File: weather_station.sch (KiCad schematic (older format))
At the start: 32 parts, among them J1 Conn_02x10_Odd_Even, J2 Conn_02x10_Odd_Even, U3 nRF52832, Y1 FL3200037

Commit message: updates
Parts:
- added C29, C30: C_Small, Capacitors_SMD:C_0402, symbol C_Small
- added J4: Conn_Coaxial, Connectors:SMA_SMD_Jack_Straight, symbol Conn_Coaxial
- added Y2: 32.786khz, Crystals:Crystal_SMD_EuroQuartz_EQ161-2pin_3.2x1.5mm, symbol Crystal
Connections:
- net GND: now also C29.2, C30.1, J4.2 (Ext)
- net RADIO_DATA: now also U3.18 (P0.15/TRACEDATA[2]); no longer U3.17 (P0.14/TRACEDATA[3])
- net RADIO_PTT: now also U3.17 (P0.14/TRACEDATA[3]); no longer U3.16 (P0.13)
- net RADIO_UART_RX: now also U3.20 (P0.17); no longer U3.19 (P0.16/TRACEDATA[1])
- net RADIO_UART_TX: now also U3.19 (P0.16/TRACEDATA[1]); no longer U3.18 (P0.15/TRACEDATA[2])
- net ANEOMETER: now reaches U3.10 (P0.08)
- net XL1: now reaches U3.2 (P0.00/XL1)
- net XL1: now also C30.2, Y2.2
- net XL2: now reaches U3.3 (P0.01/XL2)
- net XL2: now also C29.1, Y2.1
- net at C12.2, L3.1, L4.2: now also J4.1 (In)
- new net RADIO_PD: U3.16 (P0.13)
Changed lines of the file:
@@
 $EndComp
 Wire Wire Line
-	7740 1530 7660 1530
+	7100 1530 7740 1530
 Wire Wire Line
 	7660 1510 7660 1600
@@
 Text GLabel 10550 2900 1    60   Input ~ 0
 SWDIO
-Text GLabel 6900 4400 2    60   Input ~ 0
+Text GLabel 6900 4300 2    60   Input ~ 0
 RADIO_UART_TX
-Text GLabel 6900 4300 2    60   Input ~ 0
+Text GLabel 6900 4200 2    60   Input ~ 0
 RADIO_UART_RX
 Text GLabel 10400 4600 1    60   Input ~ 0
@@
 	0    1    1    0
 $EndComp
-Text GLabel 6900 4600 2    60   Input ~ 0
+Text GLabel 6900 4500 2    60   Input ~ 0
 RADIO_PTT
 Text GLabel 6900 2900 2    60   Input ~ 0
@@
 Entry Wire Line
 	-450 4100 -350 4200
-Text GLabel 6900 4500 2    60   Input ~ 0
+Text GLabel 6900 4400 2    60   Input ~ 0
 RADIO_DATA
 Text GLabel 6900 4700 2    60   Input ~ 0
@@
 Text GLabel 6900 3600 2    60   Input ~ 0
 SWDIO
+Text GLabel 6900 4600 2    60   Input ~ 0
+RADIO_PD
+$Comp
+L Crystal Y2
+U 1 1 5A788BD1
+P 2300 3550
+F 0 "Y2" H 2300 3700 50  0000 C CNN
+F 1 "32.786khz" H 2300 3400 50  0000 C CNN
+F 2 "Crystals:Crystal_SMD_EuroQuartz_EQ161-2pin_3.2x1.5mm" H 2300 3550 50  0001 C CNN
+F 3 "" H 2300 3550 50  0001 C CNN
+	1    2300 3550
+	1    0    0    -1
+$EndComp
+Text GLabel 2500 3500 1    60   Input ~ 0
+XL1
+Text GLabel 2050 3500 1    60   Input ~ 0
+XL2
+Wire Wire Line
+	2450 3550 2550 3550
+Wire Wire Line
+	2500 3550 2500 3500
+$Comp
+L C_Small C30
+U 1 1 5A7892B3
+P 2650 3550
+F 0 "C30" H 2660 3620 50  0000 L CNN
+F 1 "C_Small" H 2660 3470 50  0000 L CNN
+F 2 "Capacitors_SMD:C_0402" H 2650 3550 50  0001 C CNN
+F 3 "" H 2650 3550 50  0001 C CNN
+	1    2650 3550
+	0    1    1    0
+$EndComp
+Connection ~ 2500 3550
+$Comp
+L C_Small C29
+U 1 1 5A789395
+P 1900 3550
+F 0 "C29" H 1910 3620 50  0000 L CNN
+F 1 "C_Small" H 1910 3470 50  0000 L CNN
+F 2 "Capacitors_SMD:C_0402" H 1900 3550 50  0001 C CNN
+F 3 "" H 1900 3550 50  0001 C CNN
+	1    1900 3550
+	0    1    1    0
+$EndComp
+Wire Wire Line
+	2050 3500 2050 3550
+Wire Wire Line
+	2000 3550 2150 3550
+Connection ~ 2050 3550
+$Comp
+L GND #PWR026
+U 1 1 5A78955B
+P 1800 3550
+F 0 "#PWR026" H 1800 3300 50  0001 C CNN
+F 1 "GND" H 1800 3400 50  0000 C CNN
+F 2 "" H 1800 3550 50  0001 C CNN
+F 3 "" H 1800 3550 50  0001 C CNN
+	1    1800 3550
+	0    1    1    0
+$EndComp
+Text GLabel 4700 3400 0    60   Input ~ 0
+XL1
+Text GLabel 4700 3500 0    60   Input ~ 0
+XL2
+$Comp
+L GND #PWR027
+U 1 1 5A78A3C0
+P 2750 3550
+F 0 "#PWR027" H 2750 3300 50  0001 C CNN
+F 1 "GND" H 2750 3400 50  0000 C CNN
+F 2 "" H 2750 3550 50  0001 C CNN
+F 3 "" H 2750 3550 50  0001 C CNN
+	1    2750 3550
+	0    -1   -1   0
+$EndComp
+$Comp
+L Conn_Coaxial J4
+U 1 1 5A78AAFF
+P 6950 1530
+F 0 "J4" H 6960 1650 50  0000 C CNN
+F 1 "Conn_Coaxial" V 7065 1530 50  0000 C CNN
+F 2 "Connectors:SMA_SMD_Jack_Straight" H 6950 1530 50  0001 C CNN
+F 3 "" H 6950 1530 50  0001 C CNN
+	1    6950 1530
+	-1   0    0    1
+$EndComp
+$Comp
+L GND #PWR028
+U 1 1 5A78B589
+P 6950 1330
+F 0 "#PWR028" H 6950 1080 50  0001 C CNN
+F 1 "GND" H 6950 1180 50  0000 C CNN
+F 2 "" H 6950 1330 50  0001 C CNN
+F 3 "" H 6950 1330 50  0001 C CNN
+	1    6950 1330
+	-1   0    0    1
+$EndComp
+Text GLabel 4700 4200 0    60   Input ~ 0
+ANEOMETER
 $EndSCHEMATC

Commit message: basing solar power supply off of openMPPT
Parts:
- AE1: footprint 24ghztraceantenna:PCB_IF_ANT_2.4G -> Microwave:SMA
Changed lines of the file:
@@
 LIBS:nxp_armmcu
 LIBS:sensors
+LIBS:SFUSat-power
 LIBS:weather_station-cache
+LIBS:OpenMPPT-cache
 EELAYER 25 0
 EELAYER END
@@
 F 0 "AE1" H 7305 1345 50  0000 R CNN
 F 1 "ant" H 7305 1270 50  0001 R CNN
-F 2 "24ghztraceantenna:PCB_IF_ANT_2.4G" H 7380 1270 50  0001 C CNN
+F 2 "Microwave:SMA" H 7380 1270 50  0001 C CNN
 F 3 "" H 7380 1270 50  0001 C CNN
 	1    7380 1170

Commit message: almost done
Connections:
- net GND: now also J2.10 (Pin_10), J2.12 (Pin_12), J2.14 (Pin_14), J2.16 (Pin_16), J2.18 (Pin_18), J2.2 (Pin_2), J2.20 (Pin_20), J2.4 (Pin_4), J2.6 (Pin_6), J2.8 (Pin_8)
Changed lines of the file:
@@
 LIBS:SFUSat-power
 LIBS:weather_station-cache
-LIBS:OpenMPPT-cache
 EELAYER 25 0
 EELAYER END
@@
 Text GLabel 6900 3100 2    60   Input ~ 0
 CS_ADS1120
-Text GLabel 7900 3050 2    60   Input ~ 0
-SCL
-Text GLabel 7900 3150 2    60   Input ~ 0
-SDA
 $Sheet
 S 5200 5600 1100 600
@@
 Text GLabel 4700 4200 0    60   Input ~ 0
 ANEOMETER
+$Comp
+L GND #PWR?
+U 1 1 5A782794
+P 10950 3400
+F 0 "#PWR?" H 10950 3150 50  0001 C CNN
+F 1 "GND" H 10950 3250 50  0000 C CNN
+F 2 "" H 10950 3400 50  0001 C CNN
+F 3 "" H 10950 3400 50  0001 C CNN
+	1    10950 3400
+	1    0    0    -1
+$EndComp
+$Comp
+L GND #PWR?
+U 1 1 5A782910
+P 10850 3400
+F 0 "#PWR?" H 10850 3150 50  0001 C CNN
+F 1 "GND" H 10850 3250 50  0000 C CNN
+F 2 "" H 10850 3400 50  0001 C CNN
+F 3 "" H 10850 3400 50  0001 C CNN
+	1    10850 3400
+	1    0    0    -1
+$EndComp
+$Comp
+L GND #PWR?
+U 1 1 5A78296C
+P 10750 3400
+F 0 "#PWR?" H 10750 3150 50  0001 C CNN
+F 1 "GND" H 10750 3250 50  0000 C CNN
+F 2 "" H 10750 3400 50  0001 C CNN
+F 3 "" H 10750 3400 50  0001 C CNN
+	1    10750 3400
+	1    0    0    -1
+$EndComp
+$Comp
+L GND #PWR?
+U 1 1 5A7829C8
+P 10650 3400
+F 0 "#PWR?" H 10650 3150 50  0001 C CNN
+F 1 "GND" H 10650 3250 50  0000 C CNN
+F 2 "" H 10650 3400 50  0001 C CNN
+F 3 "" H 10650 3400 50  0001 C CNN
+	1    10650 3400
+	1    0    0    -1
+$EndComp
+$Comp
+L GND #PWR?
+U 1 1 5A782A24
+P 10550 3400
+F 0 "#PWR?" H 10550 3150 50  0001 C CNN
+F 1 "GND" H 10550 3250 50  0000 C CNN
+F 2 "" H 10550 3400 50  0001 C CNN
+F 3 "" H 10550 3400 50  0001 C CNN
+	1    10550 3400
+	1    0    0    -1
+$EndComp
+$Comp
+L GND #PWR?
+U 1 1 5A782A80
+P 10450 3400
+F 0 "#PWR?" H 10450 3150 50  0001 C CNN
+F 1 "GND" H 10450 3250 50  0000 C CNN
+F 2 "" H 10450 3400 50  0001 C CNN
+F 3 "" H 10450 3400 50  0001 C CNN
+	1    10450 3400
+	1    0    0    -1
+$EndComp
+$Comp
+L GND #PWR?
+U 1 1 5A782ADC
+P 10350 3400
+F 0 "#PWR?" H 10350 3150 50  0001 C CNN
+F 1 "GND" H 10350 3250 50  0000 C CNN
+F 2 "" H 10350 3400 50  0001 C CNN
+F 3 "" H 10350 3400 50  0001 C CNN
+	1    10350 3400
+	1    0    0    -1
+$EndComp
+$Comp
+L GND #PWR?
+U 1 1 5A782B5C
+P 10250 3400
+F 0 "#PWR?" H 10250 3150 50  0001 C CNN
+F 1 "GND" H 10250 3250 50  0000 C CNN
+F 2 "" H 10250 3400 50  0001 C CNN
+F 3 "" H 10250 3400 50  0001 C CNN
+	1    10250 3400
+	1    0    0    -1
+$EndComp
+$Comp
+L GND #PWR?
+U 1 1 5A782BB8
+P 10150 3400
+F 0 "#PWR?" H 10150 3150 50  0001 C CNN
+F 1 "GND" H 10150 3250 50  0000 C CNN
+F 2 "" H 10150 3400 50  0001 C CNN
+F 3 "" H 10150 3400 50  0001 C CNN
+	1    10150 3400
+	1    0    0    -1
+$EndComp
+$Comp
+L GND #PWR?
+U 1 1 5A782C14
+P 10050 3400
+F 0 "#PWR?" H 10050 3150 50  0001 C CNN
+F 1 "GND" H 10050 3250 50  0000 C CNN
+F 2 "" H 10050 3400 50  0001 C CNN
+F 3 "" H 10050 3400 50  0001 C CNN
+	1    10050 3400
+	1    0    0    -1
+$EndComp
 $EndSCHEMATC

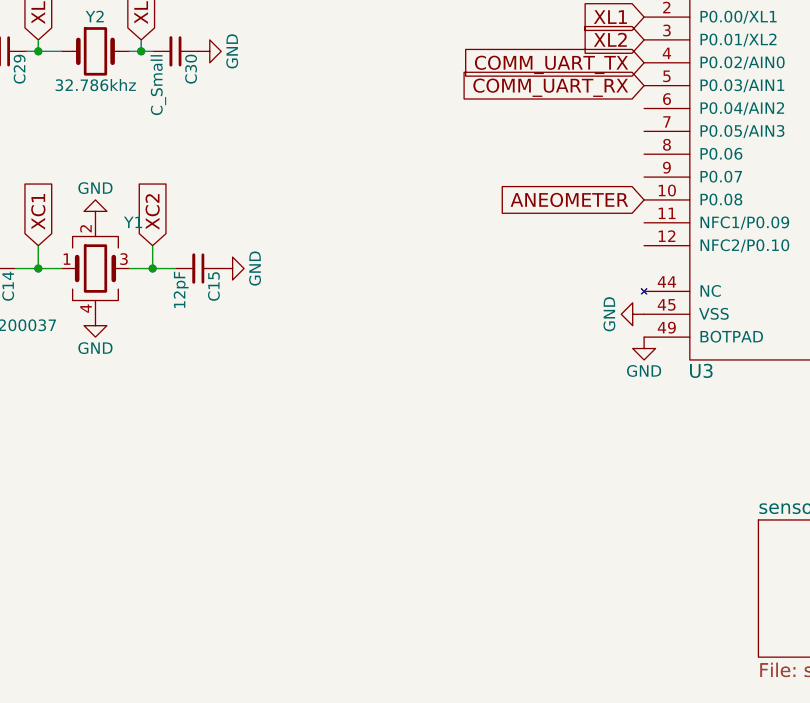
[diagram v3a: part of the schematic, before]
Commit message: might as well be able to monitor battery voltage from the nrf52832
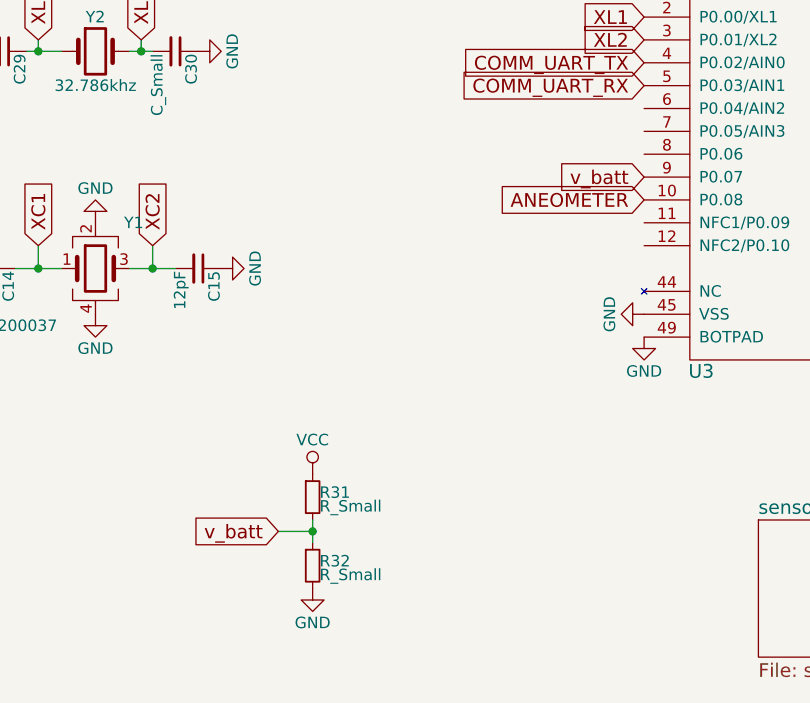
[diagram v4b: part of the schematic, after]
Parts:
- added R31, R32: R_Small, Resistors_SMD:R_0603, symbol R_Small
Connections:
- net GND: now also R32.2
- net VCC: now also R31.1
- net v_batt: now reaches U3.9 (P0.07)
- net v_batt: now also R31.2, R32.1

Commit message: i think that's enough for now
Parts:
- removed D1: D_Zener, Diodes_SMD:D_0603, symbol D_Zener
- C12, C13: value C_Small -> tuning_cap
- L4: value L_Small -> tuning_inductor
- R31, R32: value R_Small -> 100kΩ
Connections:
- net VCC is gone; now on net +BATT: C2.2, R31.1
- net v_batt: now also U3.7 (P0.05/AIN3); no longer U3.9 (P0.07)

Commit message: some cost savings
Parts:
- added MK9: (no value), via:via, symbol Mounting_Hole_PAD
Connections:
- net GND: now also MK9.1
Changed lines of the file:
@@
 LIBS:sensors
 LIBS:SFUSat-power
+LIBS:battery_management
 LIBS:weather_station-cache
 EELAYER 25 0
@@
 Text GLabel 6900 2500 2    60   Input ~ 0
 SPI_DRDY
-Entry Wire Line
-	-450 4150 -350 4250
-Entry Wire Line
-	-450 4100 -350 4200
 Text GLabel 6900 4400 2    60   Input ~ 0
 RADIO_DATA
@@
 Text GLabel 4700 3900 0    60   Input ~ 0
 v_batt
+$Comp
+L GND #PWR041
+U 1 1 5A7E57D6
+P 2000 6000
+F 0 "#PWR041" H 2000 5750 50  0001 C CNN
+F 1 "GND" H 2000 5850 50  0000 C CNN
+F 2 "" H 2000 6000 50  0001 C CNN
+F 3 "" H 2000 6000 50  0001 C CNN
+	1    2000 6000
+	1    0    0    -1
+$EndComp
+$Comp
+L Mounting_Hole_PAD MK9
+U 1 1 5A7E5834
+P 2000 5900
+F 0 "MK9" H 2000 6150 50  0000 C CNN
+F 1 " " H 2000 6075 50  0000 C CNN
+F 2 "via:via" H 2000 5900 50  0001 C CNN
+F 3 "" H 2000 5900 50  0001 C CNN
+	1    2000 5900
+	1    0    0    -1
+$EndComp
 $EndSCHEMATC

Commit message: some changes
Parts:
- removed J2: Conn_02x10_Odd_Even, Pin_Headers:Pin_Header_Straight_2x10_Pitch2.54mm, symbol Conn_02x10_Odd_Even
- added J2: Conn_01x06, Pin_Headers:Pin_Header_Straight_1x06_Pitch2.54mm, symbol Conn_01x06
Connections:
- net +3V3: now also J2.1 (Pin_1)
- net GND: now also J2.6 (Pin_6)
- net SCL: no longer U3.15 (P0.12)
- net SDA: no longer U3.14 (P0.11)
- net SWCLK: now also J2.2 (Pin_2)
- net SWDIO: now also J2.5 (Pin_5)
- net ANEOMETER: no longer names the net of U3.10 (P0.08)
- net CS_ADS1120 renamed PORT_25
- net CS_MPL115A1 renamed PORT_27
- net RESET: no longer names the net of U3.24 (P0.21/RESET)
- net SHDMPL115A1 renamed AIN4
- net SPI_CLK renamed PORT_26
- net SPI_DRDY renamed AIN7
- net SPI_MSI renamed AIN6
- net SPI_MSO renamed AIN5
- net SWO: no longer names the net of U3.21 (P0.18/TRACEDATA[0])
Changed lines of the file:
@@
 $Descr A4 11693 8268
 encoding utf-8
-Sheet 1 4
+Sheet 1 3
 Title ""
 Date ""
@@
 L +3.3V #PWR019
 U 1 1 5A7630E1
-P 10950 2900
-F 0 "#PWR019" H 10950 2750 50  0001 C CNN
-F 1 "+3.3V" H 10950 3040 50  0000 C CNN
-F 2 "" H 10950 2900 50  0000 C CNN
-F 3 "" H 10950 2900 50  0000 C CNN
-	1    10950 2900
-	1    0    0    -1
-$EndComp
-Text GLabel 10750 2900 1    60   Input ~ 0
-SWO
-Text GLabel 6900 4100 2    60   Input ~ 0
-SWO
-Text GLabel 6900 3800 2    60   Input ~ 0
-RESET
-Text GLabel 10650 2900 1    60   Input ~ 0
-RESET
+P 9650 3150
+F 0 "#PWR019" H 9650 3000 50  0001 C CNN
+F 1 "+3.3V" H 9650 3290 50  0000 C CNN
+F 2 "" H 9650 3150 50  0000 C CNN
+F 3 "" H 9650 3150 50  0000 C CNN
+	1    9650 3150
+	1    0    0    -1
+$EndComp
 Wire Wire Line
 	2050 4400 2050 4500
@@
 	0    1    1    0
 $EndComp
-Text GLabel 10850 2900 1    60   Input ~ 0
+Text GLabel 9550 3150 1    60   Input ~ 0
 SWCLK
-Text GLabel 10550 2900 1    60   Input ~ 0
+Text GLabel 9250 3150 1    60   Input ~ 0
 SWDIO
 Text GLabel 6900 4300 2    60   Input ~ 0
@@
 F1 "power.sch" 60
 $EndSheet
-$Comp
-L Conn_02x10_Odd_Even J2
-U 1 1 5A76488A
-P 10550 3100
-F 0 "J2" H 10600 3600 50  0000 C CNN
-F 1 "Conn_02x10_Odd_Even" H 10600 2500 50  0000 C CNN
-F 2 "Pin_Headers:Pin_Header_Straight_2x10_Pitch2.54mm" H 10550 3100 50  0001 C CNN
-F 3 "" H 10550 3100 50  0001 C CNN
-	1    10550 3100
-	0    1    1    0
-$EndComp
 Text GLabel 6900 4500 2    60   Input ~ 0
 RADIO_PTT
-Text GLabel 6900 2900 2    60   Input ~ 0
-CS_MPL115A1
-Text GLabel 6900 2800 2    60   Input ~ 0
-SHDMPL115A1
-Text GLabel 6900 3100 2    60   Input ~ 0
-CS_ADS1120
-$Sheet
-S 5200 5600 1100 600
-U 5A776951
-F0 "sensors" 60
-F1 "sensors.sch" 60
-$EndSheet
-Text GLabel 6900 3000 2    60   Input ~ 0
-SPI_CLK
-Text GLabel 6900 2700 2    60   Input ~ 0
-SPI_MSO
-Text GLabel 6900 2600 2    60   Input ~ 0
-SPI_MSI
-Text GLabel 6900 2500 2    60   Input ~ 0
-SPI_DRDY
 Text GLabel 6900 4400 2    60   Input ~ 0
 RADIO_DATA
-Text GLabel 6900 4700 2    60   Input ~ 0
-SCL
-Text GLabel 6900 4800 2    60   Input ~ 0
-SDA
-Text GLabel 6900 3700 2    60   Input ~ 0
-SWCLK
-Text GLabel 6900 3600 2    60   Input ~ 0
-SWDIO
 Text GLabel 6900 4600 2    60   Input ~ 0
 RADIO_PD
@@
 	-1   0    0    1
 $EndComp
-Text GLabel 4700 4200 0    60   Input ~ 0
-ANEOMETER
 $Comp
 L GND #PWR029
-U 1 1 5A782794
-P 10950 3400
-F 0 "#PWR029" H 10950 3150 50  0001 C CNN
-F 1 "GND" H 10950 3250 50  0000 C CNN
-F 2 "" H 10950 3400 50  0001 C CNN
-F 3 "" H 10950 3400 50  0001 C CNN
-	1    10950 3400
-	1    0    0    -1
-$EndComp
-$Comp
-L GND #PWR030
-U 1 1 5A782910
-P 10850 3400
-F 0 "#PWR030" H 10850 3150 50  0001 C CNN
-F 1 "GND" H 10850 3250 50  0000 C CNN
-F 2 "" H 10850 3400 50  0001 C CNN
-F 3 "" H 10850 3400 50  0001 C CNN
-	1    10850 3400
-	1    0    0    -1
-$EndComp
-$Comp
-L GND #PWR031
-U 1 1 5A78296C
-P 10750 3400
-F 0 "#PWR031" H 10750 3150 50  0001 C CNN
-F 1 "GND" H 10750 3250 50  0000 C CNN
-F 2 "" H 10750 3400 50  0001 C CNN
-F 3 "" H 10750 3400 50  0001 C CNN
-	1    10750 3400
-	1    0    0    -1
-$EndComp
-$Comp
-L GND #PWR032
-U 1 1 5A7829C8
-P 10650 3400
-F 0 "#PWR032" H 10650 3150 50  0001 C CNN
-F 1 "GND" H 10650 3250 50  0000 C CNN
-F 2 "" H 10650 3400 50  0001 C CNN
-F 3 "" H 10650 3400 50  0001 C CNN
-	1    10650 3400
-	1    0    0    -1
-$EndComp
-$Comp
-L GND #PWR033
-U 1 1 5A782A24
-P 10550 3400
-F 0 "#PWR033" H 10550 3150 50  0001 C CNN
-F 1 "GND" H 10550 3250 50  0000 C CNN
-F 2 "" H 10550 3400 50  0001 C CNN
-F 3 "" H 10550 3400 50  0001 C CNN
-	1    10550 3400
-	1    0    0    -1
-$EndComp
-$Comp
-L GND #PWR034
-U 1 1 5A782A80
-P 10450 3400
-F 0 "#PWR034" H 10450 3150 50  0001 C CNN
-F 1 "GND" H 10450 3250 50  0000 C CNN
-F 2 "" H 10450 3400 50  0001 C CNN
-F 3 "" H 10450 3400 50  0001 C CNN
-	1    10450 3400
-	1    0    0    -1
-$EndComp
-$Comp
-L GND #PWR035
-U 1 1 5A782ADC
-P 10350 3400
-F 0 "#PWR035" H 10350 3150 50  0001 C CNN
-F 1 "GND" H 10350 3250 50  0000 C CNN
-F 2 "" H 10350 3400 50  0001 C CNN
-F 3 "" H 10350 3400 50  0001 C CNN
-	1    10350 3400
-	1    0    0    -1
-$EndComp
-$Comp
-L GND #PWR036
-U 1 1 5A782B5C
-P 10250 3400
-F 0 "#PWR036" H 10250 3150 50  0001 C CNN
-F 1 "GND" H 10250 3250 50  0000 C CNN
-F 2 "" H 10250 3400 50  0001 C CNN
-F 3 "" H 10250 3400 50  0001 C CNN
-	1    10250 3400
-	1    0    0    -1
-$EndComp
-$Comp
-L GND #PWR037
-U 1 1 5A782BB8
-P 10150 3400
-F 0 "#PWR037" H 10150 3150 50  0001 C CNN
-F 1 "GND" H 10150 3250 50  0000 C CNN
-F 2 "" H 10150 3400 50  0001 C CNN
-F 3 "" H 10150 3400 50  0001 C CNN
-	1    10150 3400
-	1    0    0    -1
-$EndComp
-$Comp
-L GND #PWR038
 U 1 1 5A782C14
-P 10050 3400
-F 0 "#PWR038" H 10050 3150 50  0001 C CNN
-F 1 "GND" H 10050 3250 50  0000 C CNN
-F 2 "" H 10050 3400 50  0001 C CNN
-F 3 "" H 10050 3400 50  0001 C CNN
-	1    10050 3400
-	1    0    0    -1
+P 9150 3150
+F 0 "#PWR029" H 9150 2900 50  0001 C CNN
+F 1 "GND" H 9150 3000 50  0000 C CNN
+F 2 "" H 9150 3150 50  0001 C CNN
+F 3 "" H 9150 3150 50  0001 C CNN
+	1    9150 3150
+	-1   0    0    1
 $EndComp
 $Comp
@@
 $EndComp
 $Comp
-L VCC #PWR039
+L VCC #PWR030
 U 1 1 5A784E55
 P 3250 5400
-F 0 "#PWR039" H 3250 5250 50  0001 C CNN
+F 0 "#PWR030" H 3250 5250 50  0001 C CNN
 F 1 "VCC" H 3250 5550 50  0000 C CNN
 F 2 "" H 3250 5400 50  0001 C CNN
@@
 Connection ~ 3250 5650
 $Comp
-L GND #PWR040
+L GND #PWR031
 U 1 1 5A784FDA
 P 3250 5900
-F 0 "#PWR040" H 3250 5650 50  0001 C CNN
+F 0 "#PWR031" H 3250 5650 50  0001 C CNN
 F 1 "GND" H 3250 5750 50  0000 C CNN
 F 2 "" H 3250 5900 50  0001 C CNN
@@
 v_batt
 $Comp
-L GND #PWR041
+L GND #PWR032
 U 1 1 5A7E57D6
 P 2000 6000
-F 0 "#PWR041" H 2000 5750 50  0001 C CNN
+F 0 "#PWR032" H 2000 5750 50  0001 C CNN
 F 1 "GND" H 2000 5850 50  0000 C CNN
 F 2 "" H 2000 6000 50  0001 C CNN
@@
 	1    0    0    -1
 $EndComp
+Text GLabel 6900 2500 2    60   Input ~ 0
+AIN7
+Text GLabel 6900 2600 2    60   Input ~ 0
+AIN6
+Text GLabel 6900 2700 2    60   Input ~ 0
+AIN5
+Text GLabel 6900 2800 2    60   Input ~ 0
+AIN4
+Text GLabel 6900 2900 2    60   Input ~ 0
+PORT_27
+Text GLabel 6900 3000 2    60   Input ~ 0
+PORT_26
+Text GLabel 6900 3100 2    60   Input ~ 0
+PORT_25
+$Comp
+L Conn_01x06 J2
+U 1 1 5AC307B3
+P 9450 3350
+F 0 "J2" H 9450 3650 50  0000 C CNN
+F 1 "Conn_01x06" H 9450 2950 50  0000 C CNN
+F 2 "Pin_Headers:Pin_Header_Straight_1x06_Pitch2.54mm" H 9450 3350 50  0001 C CNN
+F 3 "" H 9450 3350 50  0001 C CNN
+	1    9450 3350
+	0    1    1    0
+$EndComp
+Text GLabel 6900 3700 2    60   Input ~ 0
+SWCLK
+Text GLabel 6900 3600 2    60   Input ~ 0
+SWDIO
 $EndSCHEMATC
